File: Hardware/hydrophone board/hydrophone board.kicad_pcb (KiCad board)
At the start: 2 copper layers, 148.6 x 66 mm, 159 parts, among them J1 AudioJack3_Ground, J111 Conn_01x02, J121 Conn_01x02, J131 Conn_01x02, J141 Conn_01x02, J2 AudioJack3_Ground, J211 Conn_01x02, J221 Conn_01x02, J231 Conn_01x02, J241 Conn_01x02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

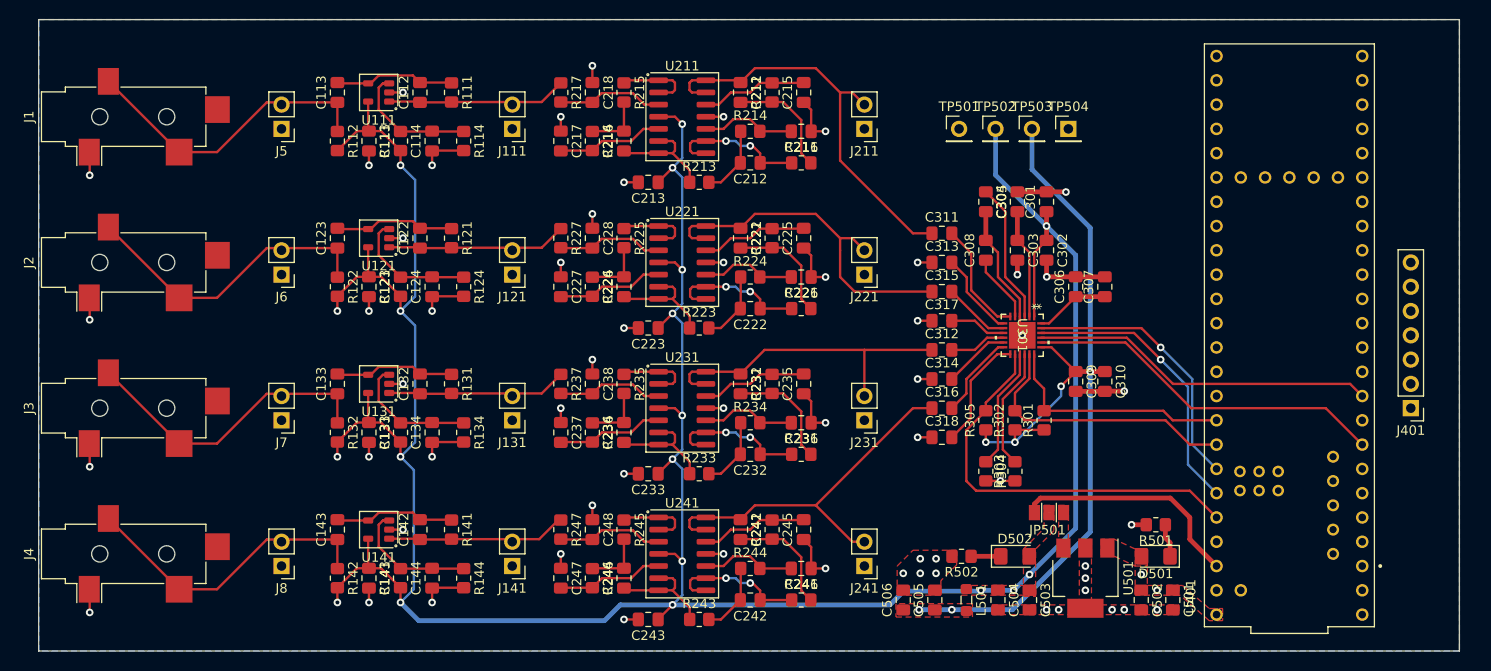
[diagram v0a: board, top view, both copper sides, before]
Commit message: changed audio jack footprint
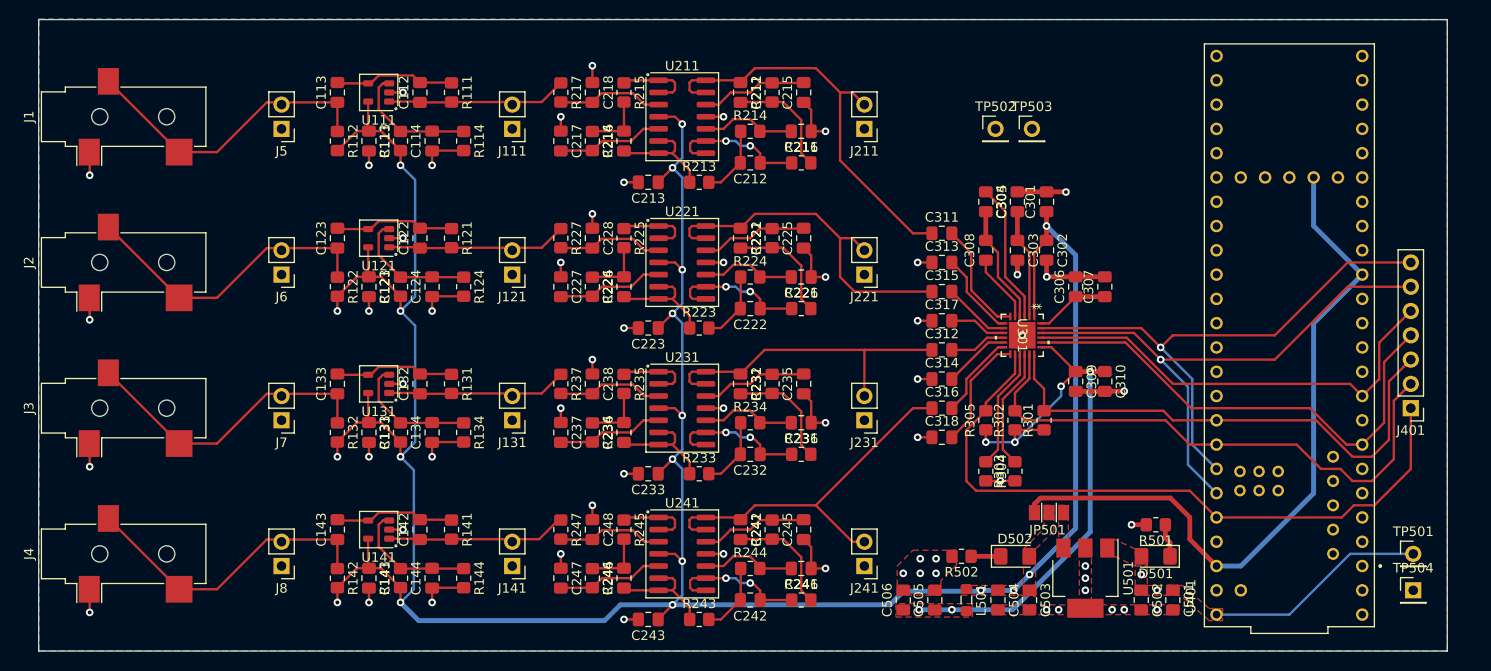
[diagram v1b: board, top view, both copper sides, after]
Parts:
- J1, J2, J3, J4: footprint Connector_Audio:Jack_3.5mm_CUI_SJ-3524-SMT_Horizontal -> Connector_Audio:Jack_3.5mm_CUI_SJ-3523-SMT_Horizontal
- moved TP501 65.1 mm to (207.3, 91.4)
- moved TP504 60.2 mm to (207.3, 95.2)
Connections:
- J5 pad 1: GND -> Net-(J5-Pin_1)
- J6 pad 1: GND -> Net-(J5-Pin_1)
- J7 pad 1: GND -> Net-(J5-Pin_1)
- J8 pad 1: GND -> Net-(J5-Pin_1)
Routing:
- net /mcu/3.3V MCU: track 24.5 -> 75.0 mm
- net /adc/FSYNC: track 28.5 -> 58.3 mm
- net /adc/SDA: track 24.8 -> 54.5 mm
- net /adc/SCL: track 29.1 -> 58.8 mm
- net /adc/BCLK: track 30.1 -> 59.4 mm
- net /adc/SHDNZ: track 43.1 -> 71.9 mm
- net +3.3VD: track 92.5 -> 64.6 mm
- net +5V: track 0.56 -> 23.8 mm
- net /adc/SDOUT_2: track 38.0 -> 51.5 mm
- net +3.3VA: track 311.3 -> 298.9 mm
- net /adc/SDOUT: track 36.1 -> 47.1 mm
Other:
- board size 148.6 x 66 mm -> 147.3 x 66 mm

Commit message: moved references, added screw holes
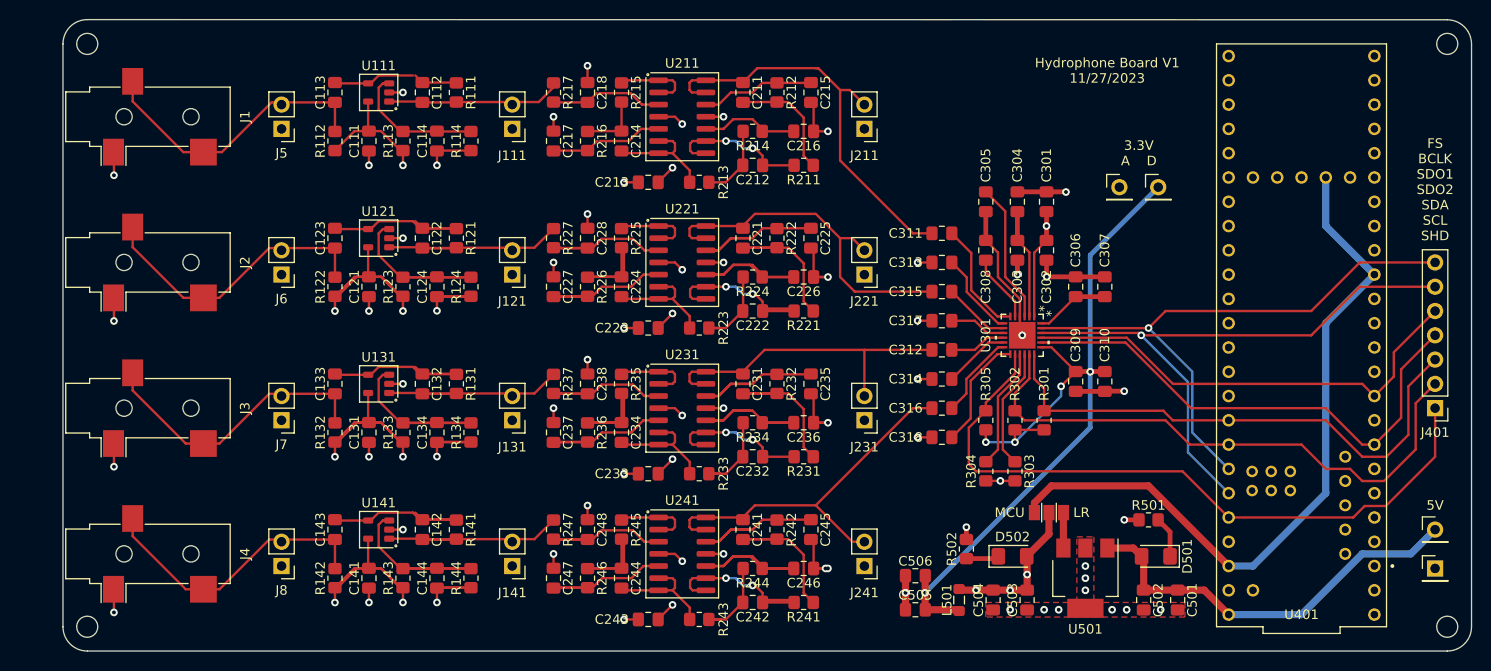
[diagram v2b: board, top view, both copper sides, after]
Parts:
- added REF**: MountingHole_2.2mm_M2, MountingHole:MountingHole_2.2mm_M2, F.Cu at (210.8, 99.1)
- added REF**: MountingHole_2.2mm_M2, MountingHole:MountingHole_2.2mm_M2, F.Cu at (68.6, 38.1)
- added REF**: MountingHole_2.2mm_M2, MountingHole:MountingHole_2.2mm_M2, F.Cu at (210.8, 38.1)
- added REF**: MountingHole_2.2mm_M2, MountingHole:MountingHole_2.2mm_M2, F.Cu at (68.6, 99.1)
- moved TP503 14.5 mm to (180.6, 53.1)
- moved TP502 14.3 mm to (176.5, 53.1)
- moved TP501 3.42 mm to (209.6, 88.9)
- moved TP504 3.23 mm to (209.6, 93.0)
- moved C506 2.84 mm to (155.2, 93.7), turned to 180 degrees
- moved J401 2.54 mm to (209.6, 76.2)
- moved J1 2.54 mm to (74.9, 45.7)
- moved J2 2.54 mm to (74.9, 61.0)
- moved J3 2.54 mm to (74.9, 76.2)
- moved J4 2.54 mm to (74.9, 91.4)
- moved C505 2.27 mm to (155.2, 97.3), turned to 180 degrees
- moved U401 1.27 mm to (195.6, 68.6)
- moved R501 0.92 mm to (179.6, 87.9)
- moved R502 0.92 mm to (160.5, 90.9), turned to 90 degrees
- moved R134 0.76 mm to (108.7, 78.7)
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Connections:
- J5 pad 1: Net-(J5-Pin_1) -> GND
- J6 pad 1: Net-(J5-Pin_1) -> GND
- J7 pad 1: Net-(J5-Pin_1) -> GND
- J8 pad 1: Net-(J5-Pin_1) -> GND
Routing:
- net +3.3VA: track 298.9 -> 130.0 mm
- net +3.3VD: track 64.6 -> 85.6 mm, vias 6 -> 5
- net +5V: track 23.8 -> 43.3 mm, vias 2 -> 0
- net GND: track 132.7 -> 151.0 mm, vias 60 -> 59
- net Net-(U221C-+): track 10.0 -> 20.3 mm
- net Net-(U241C-+): track 10.0 -> 20.3 mm
- net Net-(U231C-+): track 10.0 -> 18.9 mm
- net Net-(U141-+): track 13.4 -> 20.0 mm
- net Net-(U121-+): track 13.4 -> 20.0 mm
- net Net-(U131-+): track 13.4 -> 20.0 mm
- net Net-(C234-Pad2): track 6.36 -> 12.7 mm
- net Net-(C244-Pad2): track 6.36 -> 12.7 mm
- net Net-(C224-Pad2): track 6.36 -> 12.7 mm
- net Net-(U231D-+): track 11.2 -> 17.4 mm
- net Net-(U241D-+): track 11.2 -> 17.1 mm
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- added copper zone on In2.Cu, net +3.3VA
- added copper zone on In1.Cu, net GND
- removed copper zone on F.Cu, net +3.3VA
- removed copper zone on F.Cu, net +3.3VD
- removed copper zone on F.Cu, net +5V
- removed copper zone on B.Cu, net GND
- removed copper zone on F.Cu, net Net-(JP501-A)
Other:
- outline, holes or cut-outs redrawn
- copper layers 2 -> 4
- board text added: "3.3V A D"
- board text added: "5V"
- board text added: "FS BCLK SDO1 SDO2 SDA SCL SHD"
- board text added: "Hydrophone Board V1 11/27/2023"
- board text added: "LR"
- board text added: "MCU"
